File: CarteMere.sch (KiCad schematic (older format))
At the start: 41 parts, among them J1 Conn_01x04:LIDAR_Data, J2 Conn_01x02, J3 Conn_01x02, J4 Conn_01x03, J5 Conn_01x03, J6 Conn_01x03, J7 Conn_01x04, J8 Conn_01x04, Q1 2N7000, Q2 Q_PMOS_DGS, Q3 PMBT2222A_215, U1 TEENSY3.6, U10 R-78C5.0-1.0, U11 TMC2130, U12 TMC2130, U2 R-78C5.0-1.0, U3 AMS1117-3.3, U4 I2C_Conn, U5 VL52L0X_simple, U6 VL52L0X_simple, U7 TEENSY3.2, U8 VL52L0X_simple, U9 VL52L0X_simple

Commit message: Mise à jour
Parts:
- added D2, D3, D4, D5: LED, LED_THT:LED_D5.0mm, symbol Device:LED
- added R10, R11, R8, R9: R, Resistor_SMD:R_1206_3216Metric_Pad1.42x1.75mm_HandSolder, symbol Device:R
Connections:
- net CS_TMC2: now also U7.24 (22(A8/PWM)); no longer U7.23 (21(A7/PWM))
- net DIR_TMC1: now also U7.18 (16(A2)); no longer U7.21 (19(A5/SCL0))
- net DIR_TMC2: now also U7.21 (19(A5/SCL0)); no longer U7.25 (23(A9/PWM))
- net EN_TMC1: now also U7.20 (18(A4/SDA0)); no longer U7.18 (16(A2))
- net EN_TMC2: now also U7.25 (23(A9/PWM)); no longer U7.22 (20(A6/PWM))
- net GND: now also D2.1 (K), D3.1 (K), D4.1 (K), D5.1 (K)
- net STEP_TMC1: now also U7.22 (20(A6/PWM)); no longer U7.20 (18(A4/SDA0))
- net STEP_TMC2: now also U7.23 (21(A7/PWM)); no longer U7.24 (22(A8/PWM))
- net at U7.16 (14(A0)): now also R11.2
- net at U7.17 (15(A1)): now also R10.2
- net LED_S1: now reaches U1.11 (9(PWM/RX2))
- net LED_S1: now also R8.2
- net LED_S2: now reaches U1.12 (10(PWM/TX2))
- net LED_S2: now also R9.2
- new net: D4.2 (A), R10.1
- new net: D5.2 (A), R11.1
- new net: D2.2 (A), R8.1
- new net: D3.2 (A), R9.1
- no-connect marks 39 -> 33
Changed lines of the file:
@@
 Sheet 1 1
 Title "Carte-mère Robot"
-Date "2020-02-22"
-Rev "R1"
+Date "2020-02-26"
+Rev "R0"
 Comp "Robot Télécom Strasbourg"
 Comment1 "Arnaud Schlumberger"
@@
 Text Label 10300 1650 0    50   ~ 0
 MISO_mvnt
-Text Label 6700 1900 0    50   ~ 0
-CS_TMC1
+Text Label 6700 1400 0    50   ~ 0
+CS_TMC2
 Text Label 6700 1500 0    50   ~ 0
-CS_TMC2
-Text Label 6700 1300 0    50   ~ 0
-DIR_TMC2
-Text Label 6700 1400 0    50   ~ 0
 STEP_TMC2
-Text Label 6700 1700 0    50   ~ 0
-DIR_TMC1
-Text Label 6700 1800 0    50   ~ 0
+Text Label 6700 1600 0    50   ~ 0
 STEP_TMC1
 $Comp
@@
 Text Label 10300 1750 0    50   ~ 0
 CS_TMC2
-Text Label 6700 1600 0    50   ~ 0
+Text Label 6700 1300 0    50   ~ 0
 EN_TMC2
-Text Label 6700 2000 0    50   ~ 0
-EN_TMC1
 $Comp
 L Connector_Generic:Conn_01x03 J4
@@
 NoConn ~ 5600 1800
 NoConn ~ 5600 1900
-NoConn ~ 6700 2200
-NoConn ~ 6700 2100
 NoConn ~ 6700 1200
 Text Label 10300 2050 0    50   ~ 0
@@
 NoConn ~ 900  5650
 NoConn ~ 900  5750
-NoConn ~ 900  5850
-NoConn ~ 900  5950
 NoConn ~ 900  6050
 NoConn ~ 900  6150
@@
 NoConn ~ 2500 6350
 NoConn ~ 2500 6150
-NoConn ~ 2500 6050
-NoConn ~ 2500 5950
 NoConn ~ 2500 5850
 NoConn ~ 2500 5750
@@
 $EndComp
 NoConn ~ 900  5150
+Text Label 6700 1800 0    50   ~ 0
+EN_TMC1
+Text Label 6700 2000 0    50   ~ 0
+DIR_TMC1
+Text Label 6700 1700 0    50   ~ 0
+DIR_TMC2
+Text Label 6700 1900 0    50   ~ 0
+CS_TMC1
+$Comp
+L Device:LED D4
+U 1 1 5E56F434
+P 7750 1950
+F 0 "D4" H 7743 1695 50  0000 C CNN
+F 1 "LED" H 7743 1786 50  0000 C CNN
+F 2 "LED_THT:LED_D5.0mm" H 7750 1950 50  0001 C CNN
+F 3 "~" H 7750 1950 50  0001 C CNN
+	1    7750 1950
+	-1   0    0    1
+$EndComp
+$Comp
+L Device:R R10
+U 1 1 5E573E76
+P 7450 1950
+F 0 "R10" V 7243 1950 50  0000 C CNN
+F 1 "R" V 7334 1950 50  0000 C CNN
+F 2 "Resistor_SMD:R_1206_3216Metric_Pad1.42x1.75mm_HandSolder" V 7380 1950 50  0001 C CNN
+F 3 "~" H 7450 1950 50  0001 C CNN
+	1    7450 1950
+	0    1    1    0
+$EndComp
+$Comp
+L Device:LED D5
+U 1 1 5E57A1AF
+P 7750 2300
+F 0 "D5" H 7743 2045 50  0000 C CNN
+F 1 "LED" H 7743 2136 50  0000 C CNN
+F 2 "LED_THT:LED_D5.0mm" H 7750 2300 50  0001 C CNN
+F 3 "~" H 7750 2300 50  0001 C CNN
+	1    7750 2300
+	-1   0    0    1
+$EndComp
+$Comp
+L Device:R R11
+U 1 1 5E57A1B5
+P 7450 2300
+F 0 "R11" V 7243 2300 50  0000 C CNN
+F 1 "R" V 7334 2300 50  0000 C CNN
+F 2 "Resistor_SMD:R_1206_3216Metric_Pad1.42x1.75mm_HandSolder" V 7380 2300 50  0001 C CNN
+F 3 "~" H 7450 2300 50  0001 C CNN
+	1    7450 2300
+	0    1    1    0
+$EndComp
+Wire Wire Line
+	6700 2100 7200 2100
+Wire Wire Line
+	7200 2100 7200 1950
+Wire Wire Line
+	7200 1950 7300 1950
+Wire Wire Line
+	7300 2300 7200 2300
+Wire Wire Line
+	7200 2300 7200 2200
+Wire Wire Line
+	7200 2200 6700 2200
+$Comp
+L power:GND #PWR03
+U 1 1 5E57D682
+P 7900 1950
+F 0 "#PWR03" H 7900 1700 50  0001 C CNN
+F 1 "GND" V 7905 1822 50  0000 R CNN
+F 2 "" H 7900 1950 50  0001 C CNN
+F 3 "" H 7900 1950 50  0001 C CNN
+	1    7900 1950
+	0    -1   -1   0
+$EndComp
+$Comp
+L power:GND #PWR04
+U 1 1 5E57DAA4
+P 7900 2300
+F 0 "#PWR04" H 7900 2050 50  0001 C CNN
+F 1 "GND" V 7905 2172 50  0000 R CNN
+F 2 "" H 7900 2300 50  0001 C CNN
+F 3 "" H 7900 2300 50  0001 C CNN
+	1    7900 2300
+	0    -1   -1   0
+$EndComp
+$Comp
+L Device:LED D2
+U 1 1 5E582664
+P 6450 3600
+F 0 "D2" H 6443 3345 50  0000 C CNN
+F 1 "LED" H 6443 3436 50  0000 C CNN
+F 2 "LED_THT:LED_D5.0mm" H 6450 3600 50  0001 C CNN
+F 3 "~" H 6450 3600 50  0001 C CNN
+	1    6450 3600
+	-1   0    0    1
+$EndComp
+$Comp
+L Device:R R8
+U 1 1 5E58266A
+P 6150 3600
+F 0 "R8" V 5943 3600 50  0000 C CNN
+F 1 "R" V 6034 3600 50  0000 C CNN
+F 2 "Resistor_SMD:R_1206_3216Metric_Pad1.42x1.75mm_HandSolder" V 6080 3600 50  0001 C CNN
+F 3 "~" H 6150 3600 50  0001 C CNN
+	1    6150 3600
+	0    1    1    0
+$EndComp
+$Comp
+L Device:LED D3
+U 1 1 5E583DC0
+P 6450 4000
+F 0 "D3" H 6443 3745 50  0000 C CNN
+F 1 "LED" H 6443 3836 50  0000 C CNN
+F 2 "LED_THT:LED_D5.0mm" H 6450 4000 50  0001 C CNN
+F 3 "~" H 6450 4000 50  0001 C CNN
+	1    6450 4000
+	-1   0    0    1
+$EndComp
+$Comp
+L Device:R R9
+U 1 1 5E583DC6
+P 6150 4000
+F 0 "R9" V 5943 4000 50  0000 C CNN
+F 1 "R" V 6034 4000 50  0000 C CNN
+F 2 "Resistor_SMD:R_1206_3216Metric_Pad1.42x1.75mm_HandSolder" V 6080 4000 50  0001 C CNN
+F 3 "~" H 6150 4000 50  0001 C CNN
+	1    6150 4000
+	0    1    1    0
+$EndComp
+$Comp
+L power:GND #PWR01
+U 1 1 5E5850C3
+P 6600 3600
+F 0 "#PWR01" H 6600 3350 50  0001 C CNN
+F 1 "GND" H 6605 3427 50  0000 C CNN
+F 2 "" H 6600 3600 50  0001 C CNN
+F 3 "" H 6600 3600 50  0001 C CNN
+	1    6600 3600
+	1    0    0    -1
+$EndComp
+$Comp
+L power:GND #PWR02
+U 1 1 5E585F24
+P 6600 4000
+F 0 "#PWR02" H 6600 3750 50  0001 C CNN
+F 1 "GND" V 6605 3872 50  0000 R CNN
+F 2 "" H 6600 4000 50  0001 C CNN
+F 3 "" H 6600 4000 50  0001 C CNN
+	1    6600 4000
+	0    -1   -1   0
+$EndComp
+Text Label 6000 3600 2    50   ~ 0
+LED_S1
+Text Label 900  5850 2    50   ~ 0
+LED_S1
+Text Label 900  5950 2    50   ~ 0
+LED_S2
+Text Label 6000 4000 2    50   ~ 0
+LED_S2
 $EndSCHEMATC

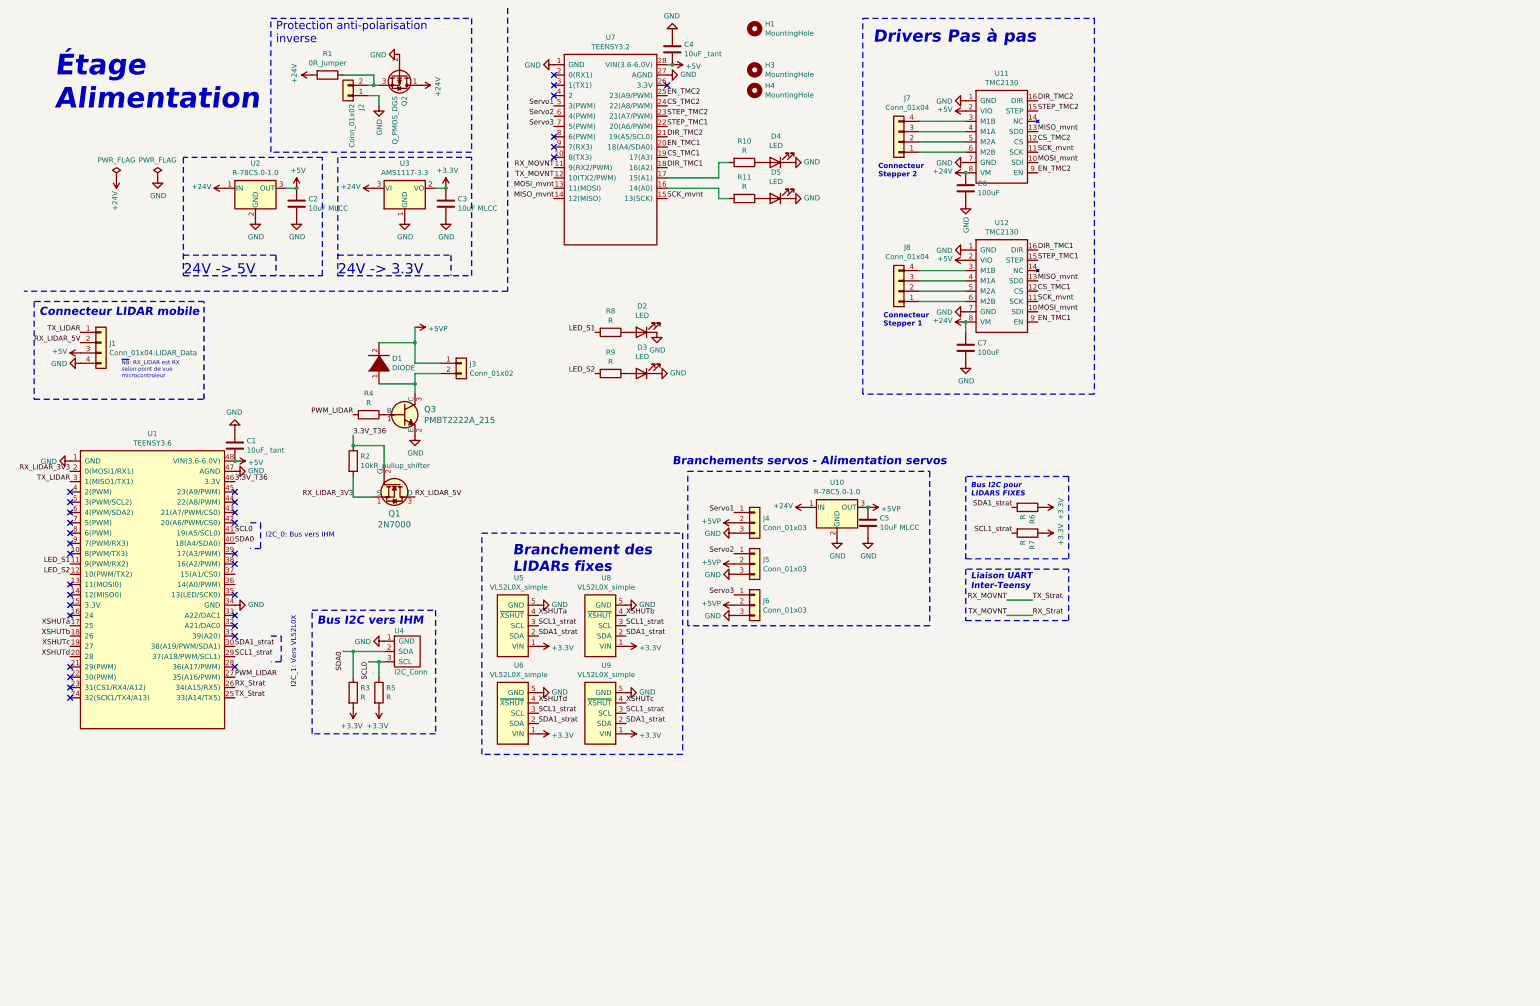
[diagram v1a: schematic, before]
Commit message: Nettoyage du schéma, ajout de l'UART 4 sur Teensy 3.6 pour debug, renforcement alimentation 5V
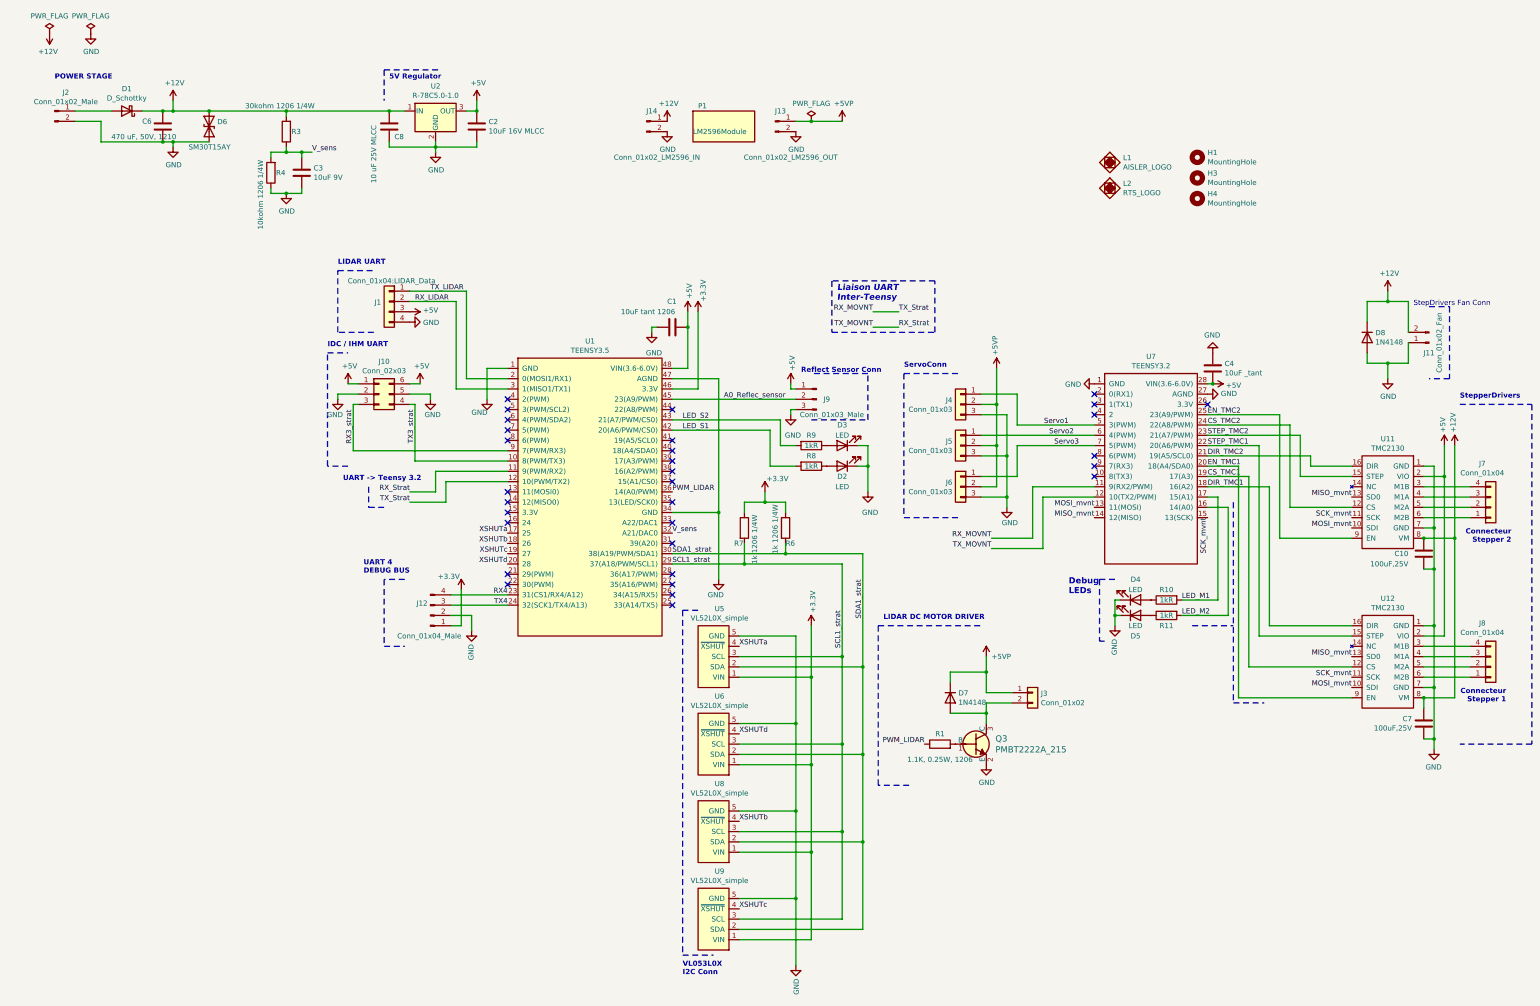
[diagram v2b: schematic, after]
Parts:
- removed C5: 10uF MLCC, Capacitor_SMD:C_1206_3216Metric_Pad1.42x1.75mm_HandSolder, symbol Device:C
- removed D1: DIODE, Diode_THT:D_DO-41_SOD81_P10.16mm_Horizontal, symbol pspice:DIODE
- removed J2: Conn_01x02, Connector_PinHeader_2.54mm:PinHeader_1x02_P2.54mm_Vertical, symbol Connector_Generic:Conn_01x02
- removed Q1: 2N7000, digikey-footprints:TO-92-3, symbol dk_Transistors-FETs-MOSFETs-Single:2N7000
- removed Q2: Q_PMOS_DGS, CFR2020_A:SOT-23_DGS_Handsoldering, symbol CFR2020_A:Q_PMOS_DGS
- removed R2: 10kR_pullup_shifter, Resistor_SMD:R_1206_3216Metric_Pad1.42x1.75mm_HandSolder, symbol Device:R
- removed R5: R, Resistor_SMD:R_1206_3216Metric_Pad1.42x1.75mm_HandSolder, symbol Device:R
- removed U10: R-78C5.0-1.0, Converter_DCDC:Converter_DCDC_RECOM_R-78E-0.5_THT, symbol Regulator_Switching:R-78C5.0-1.0
- removed U3: AMS1117-3.3, Package_TO_SOT_SMD:SOT-223-3_TabPin2, symbol Regulator_Linear:AMS1117-3.3
- removed U4: I2C_Conn, Connector_JST:JST_XH_B4B-XH-AM_1x04_P2.50mm_Vertical, symbol CFR2020_A:I2C_Conn
- added C10: 100uF,25V, Capacitor_THT:CP_Radial_D6.3mm_P2.50mm, symbol Device:C
- added C8: 10 uF 25V MLCC, Capacitor_SMD:C_1206_3216Metric_Pad1.42x1.75mm_HandSolder, symbol Device:C
- added D1: D_Schottky, Diode_SMD:D_SMA_Handsoldering, symbol Device:D_Schottky
- added D6: SM30T15AY, Diode_SMD:D_SMC_Handsoldering, symbol Device:D_TVS
- added D7, D8: 1N4148, Diode_SMD:D_SOD-123, symbol Device:D
- added J10: Conn_02x03, Connector_IDC:IDC-Header_2x03_P2.54mm_Vertical, symbol Connector_Generic:Conn_02x03_Counter_Clockwise
- added J11: Conn_01x02_Fan, Connector_JST:JST_XH_B2B-XH-A_1x02_P2.50mm_Vertical, symbol Connector:Conn_01x02_Male
- added J12: Conn_01x04_Male, Connector_JST:JST_XH_B4B-XH-AM_1x04_P2.50mm_Vertical, symbol Connector:Conn_01x04_Male
- added J13: Conn_01x02_LM2596_OUT, rex:BatConn, symbol Connector:Conn_01x02_Male
- added J14: Conn_01x02_LM2596_IN, rex:BatConn, symbol Connector:Conn_01x02_Male
- added J2: Conn_01x02_Male, CFR2020_A:OSTOQ027151, symbol Connector:Conn_01x02_Male
- added J9: Conn_01x03_Male, Connector_PinSocket_2.54mm:PinSocket_1x03_P2.54mm_Vertical, symbol Connector:Conn_01x03_Male
- added L1: AISLER_LOGO, Logo:aisler, symbol CFR2020_A:AISLER_LOGO
- added L2: RTS_LOGO, Logo:rts, symbol CFR2020_A:RTS_LOGO
- added P1: LM2596Module, CFR2020_A:LM2596 Module, symbol CFR2020_A:LM2596Module
- C1: value 10uF_ tant -> 10uF tant 1206
- C2: value 10uF MLCC -> 10uF 16V MLCC
- C3: value 10uF MLCC -> 10uF 9V
- C6: value 100uF -> 470 uF, 50V, 1210; footprint Capacitor_THT:CP_Radial_D8.0mm_P2.50mm -> Capacitor_SMD:C_1210_3225Metric_Pad1.42x2.65mm_HandSolder
- C7: value 100uF -> 100uF,25V; footprint Capacitor_THT:CP_Radial_D8.0mm_P2.50mm -> Capacitor_THT:CP_Radial_D6.3mm_P2.50mm
- D2, D3, D4, D5: footprint LED_THT:LED_D5.0mm -> LED_SMD:LED_1206_3216Metric_Pad1.42x1.75mm_HandSolder
- R1: value 0R_Jumper -> 1.1K, 0.25W, 1206
- R10, R11, R8, R9: value R -> 1kR
- R3: value R -> 30kohm 1206 1/4W
- R4: value R -> 10kohm 1206 1/4W
- R6, R7: value R -> 1k 1206 1/4W
- U1: value TEENSY3.6 -> TEENSY3.5
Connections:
- net 3.3V_T36 is gone; now on net +3V3: U1.46 (3.3V)
- net RX_LIDAR_3V3 is gone; now on net TX_LIDAR: U1.2 (0(MOSI1/RX1))
- net +3V3: now also J12.1 (Pin_1); no longer C3.1, R3.2
- net +5V: now also C1.1, J10.1 (Pin_1), J10.6 (Pin_6), J9.1 (Pin_1); no longer C1.2
- net +5VP: now also D7.1 (K), J13.1 (Pin_1)
- net GND: now also C1.2, R4.1, C10.2, C8.2, D6.2 (A2), D8.2 (A), J10.2 (Pin_2), J10.5 (Pin_5), J11.1 (Pin_1), J12.2 (Pin_2), J13.2 (Pin_2), J14.2 (Pin_2), J2.2 (Pin_2), J9.3 (Pin_3); no longer C1.1
- net LED_S1: now also U1.42 (20(A6/PWM/CS0)); no longer U1.11 (9(PWM/RX2))
- net LED_S2: now also U1.43 (21(A7/PWM/CS0)); no longer U1.12 (10(PWM/TX2))
- net PWM_LIDAR: now also R1.1, U1.36 (14(A0/PWM)); no longer R4.2, U1.27 (35(A16/PWM))
- net RX_MOVNT: now also U1.12 (10(PWM/TX2)); no longer U1.25 (33(A14/TX5))
- net RX_Strat: now also U1.11 (9(PWM/RX2)); no longer U1.26 (34(A15/RX5))
- net TX_LIDAR: no longer U1.3 (1(MISO1/TX1))
- net LED_M2: now reaches R11.2, U7.16 (14(A0))
- net LED_M1: now reaches R10.2, U7.17 (15(A1))
- net TX3_strat: now reaches U1.10 (8(PWM/TX3))
- net TX3_strat: now also J10.4 (Pin_4)
- net RX4: now reaches U1.23 (31(CS1/RX4/A12))
- net RX4: now also J12.4 (Pin_4)
- net TX4: now reaches U1.24 (32(SCK1/TX4/A13))
- net TX4: now also J12.3 (Pin_3)
- net V_sens: now reaches U1.32 (A21/DAC0)
- net V_sens: now also C3.1, R3.1, R4.2
- net A0_Reflec_sensor: now reaches U1.45 (23(A9/PWM))
- net A0_Reflec_sensor: now also J9.2 (Pin_2)
- net RX3_strat: now reaches U1.9 (7(PWM/RX3))
- net RX3_strat: now also J10.3 (Pin_3)
- net at Q3.1 (B): now also R1.2; no longer R4.1
- net at J3.2 (Pin_2), Q3.3 (C): now also D7.2 (A)
- net +24V renamed +12V
- net +12V: now also R3.2, C10.1, C8.1, D1.1 (K), D6.1 (A1), D8.1 (K), J11.2 (Pin_2), J14.1 (Pin_1); no longer R1.2
- net RX_LIDAR_5V renamed RX_LIDAR
- net RX_LIDAR: now also U1.3 (1(MISO1/TX1))
- net SCL0: no longer names the net of U1.41 (19(A5/SCL0))
- net SDA0: no longer names the net of U1.40 (18(A4/SDA0))
- net SDA0: no longer R3.1
- new net: D1.2 (A), J2.1 (Pin_1)
- no-connect marks 33 -> 31
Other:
- note added: "5V Regulator"
- note added: "Debug\nLEDs\n"
- note added: "IDC / IHM UART"
- note added: "LIDAR DC MOTOR DRIVER"
- note added: "LIDAR UART"
- note added: "POWER STAGE"
- note added: "Reflect Sensor Conn"
- note added: "ServoConn"
- note added: "StepDrivers Fan Conn"
- note added: "StepperDrivers"
- note added: "UART -> Teensy 3.2"
- note added: "UART 4\nDEBUG BUS"
- note added: "VL053L0X\nI2C Conn"
- note removed: "24V -> 3.3V"
- note removed: "24V -> 5V"
- note removed: "Branchement des \nLIDARs fixes\n\n"
- note removed: "Branchements servos - Alimentation servos"
- note removed: "Bus I2C pour\nLIDARS FIXES"
- note removed: "Bus I2C vers IHM"
- note removed: "Connecteur LIDAR mobile"
- note removed: "Drivers Pas à pas"
- note removed: "I2C_0: Bus vers IHM"
- note removed: "I2C_1: Vers VL52L0X\n"
- note removed: "Protection anti-polarisation\ninverse\n"
- note removed: "~NB~: RX_LIDAR est RX \nselon point de vue\nmicrocontroleur"
- note removed: "Étage \nAlimentation\n"
- moved on the sheet: C1, C2, C4, C7, D2, D3, D4, D5, H1, H3, H4, J1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
